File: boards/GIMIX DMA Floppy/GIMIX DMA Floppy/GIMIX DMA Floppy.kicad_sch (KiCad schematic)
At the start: 24 parts, among them P1 SS-50 Bus, U10 74LS393, U11 7404, U14 74LS08, U23 7406, U24 74LS74, U25 74LS74, U27 74LS138, U28 74LS273, U29 74LS174, U34 74LS240, U35 74LS240, U36 74F04, U37 7420, U38 74LS367, U39 74LS32, U41 74LS136, U47 74LS533, U48 74LS244, U6 74LS08, U7 74LS08

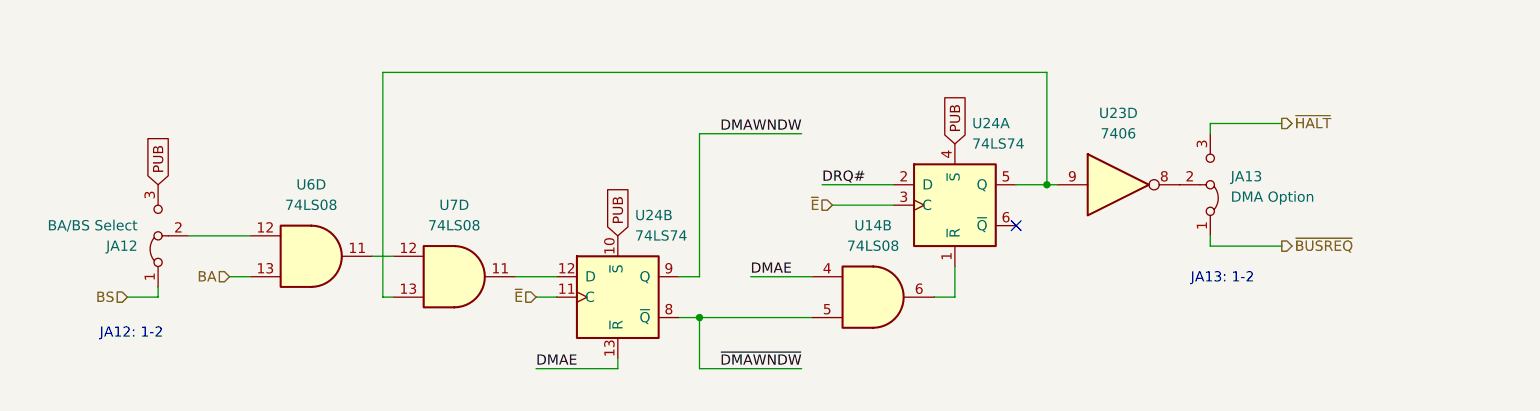
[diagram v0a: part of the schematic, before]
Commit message: DMA Floppy update, silkscreen and gerbers added
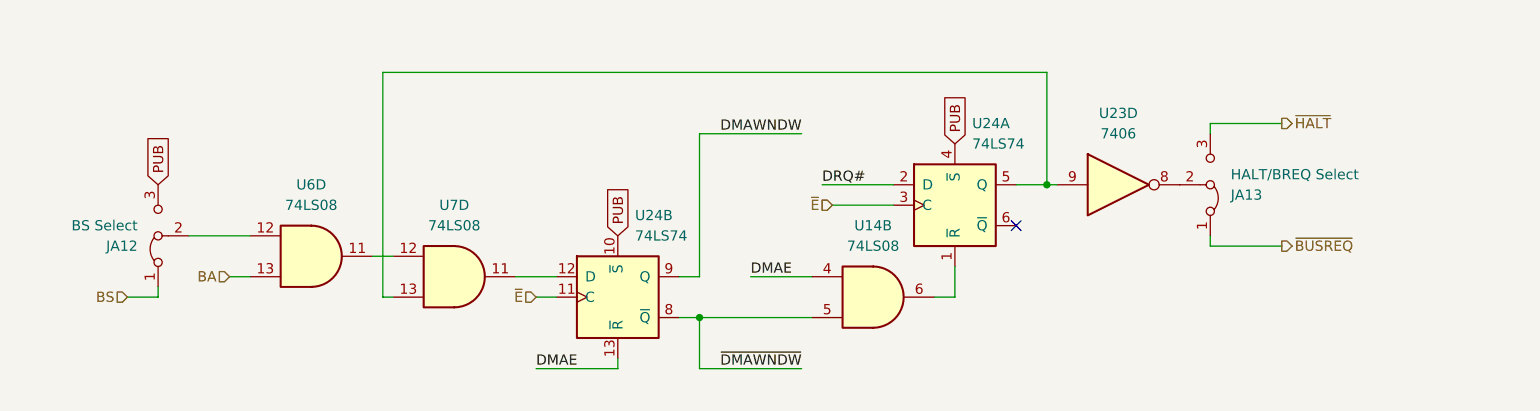
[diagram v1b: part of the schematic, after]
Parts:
- JA12: value BA/BS Select -> BS Select
- JA13: value DMA Option -> HALT/BREQ Select
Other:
- note removed: "JA12: 1-2"
- note removed: "JA13: 1-2"
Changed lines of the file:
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@@
 		)
 	)
-	(text "JA13: 1-2"
-		(exclude_from_sim no)
-		(at 161.544 266.954 0)
-		(effects
-			(font
-				(size 1.27 1.27)
-			)
-		)
-	)
 	(text "on GIMIX\nBE and BQ\nare inverted.\nCheck with CMS!"
 		(exclude_from_sim no)
@@
 		)
 	)
-	(text "JA12: 1-2"
-		(exclude_from_sim no)
-		(at 25.908 273.812 0)
-		(effects
-			(font
-				(size 1.27 1.27)
-			)
-		)
-	)
 	(text "FDC Data"
 		(exclude_from_sim no)
@@
 			)
 		)
-		(property "Value" "BA/BS Select"
+		(property "Value" "BS Select"
 			(at 26.67 260.3501 90)
 			(effects
@@
 		(dnp no)
 		(property "Reference" "JA13"
-			(at 162.56 254.254 90)
+			(at 162.56 256.5401 90)
 			(effects
 				(font
@@
 			)
 		)
-		(property "Value" "DMA Option"
-			(at 162.56 256.794 90)
+		(property "Value" "HALT/BREQ Select"
+			(at 162.56 254.0001 90)
 			(effects
 				(font
